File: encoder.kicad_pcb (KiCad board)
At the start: 2 copper layers, 20 x 15 mm, 13 parts, among them IC1 AS5048

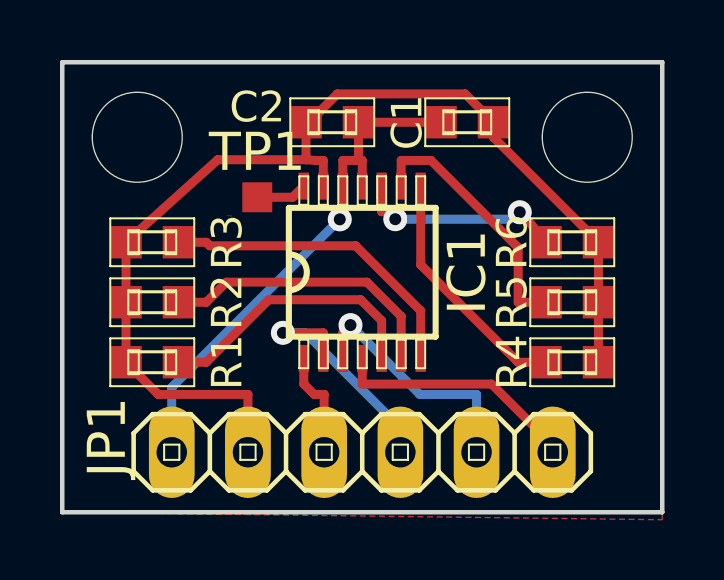
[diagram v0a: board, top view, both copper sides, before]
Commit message: Add panelized PCB data
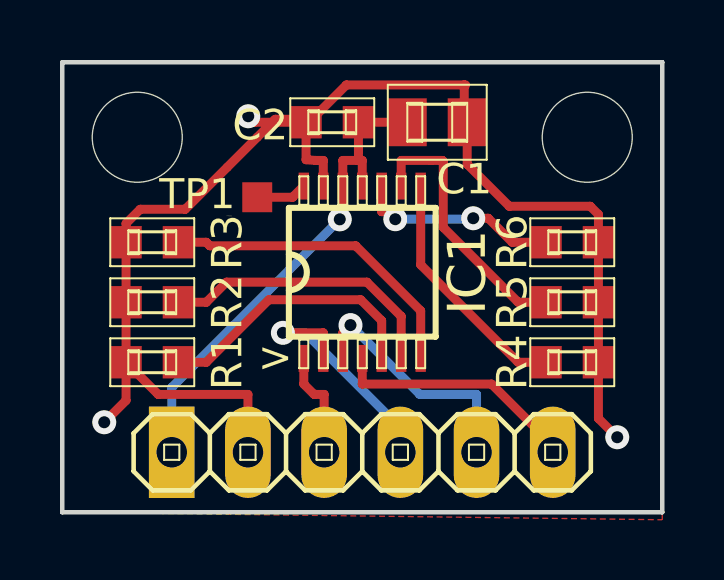
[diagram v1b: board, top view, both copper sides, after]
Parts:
- C1: footprint generic:generic-SMD1608 -> generic:generic-SMD2012
- moved C1 1.00 mm to (147.5, 92.0)
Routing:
- net GNDD: track 37.1 -> 47.7 mm, vias 0 -> 3
- net +3V3: track 18.5 -> 17.5 mm
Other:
- board text added: ">"
- board text added: "Encoder v1.3"
- board text removed: "Encoder v1.1"
